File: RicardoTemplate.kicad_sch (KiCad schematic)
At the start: 39 parts, among them J1 RBUS, U1 ESP32-S3, Y1 R940000171

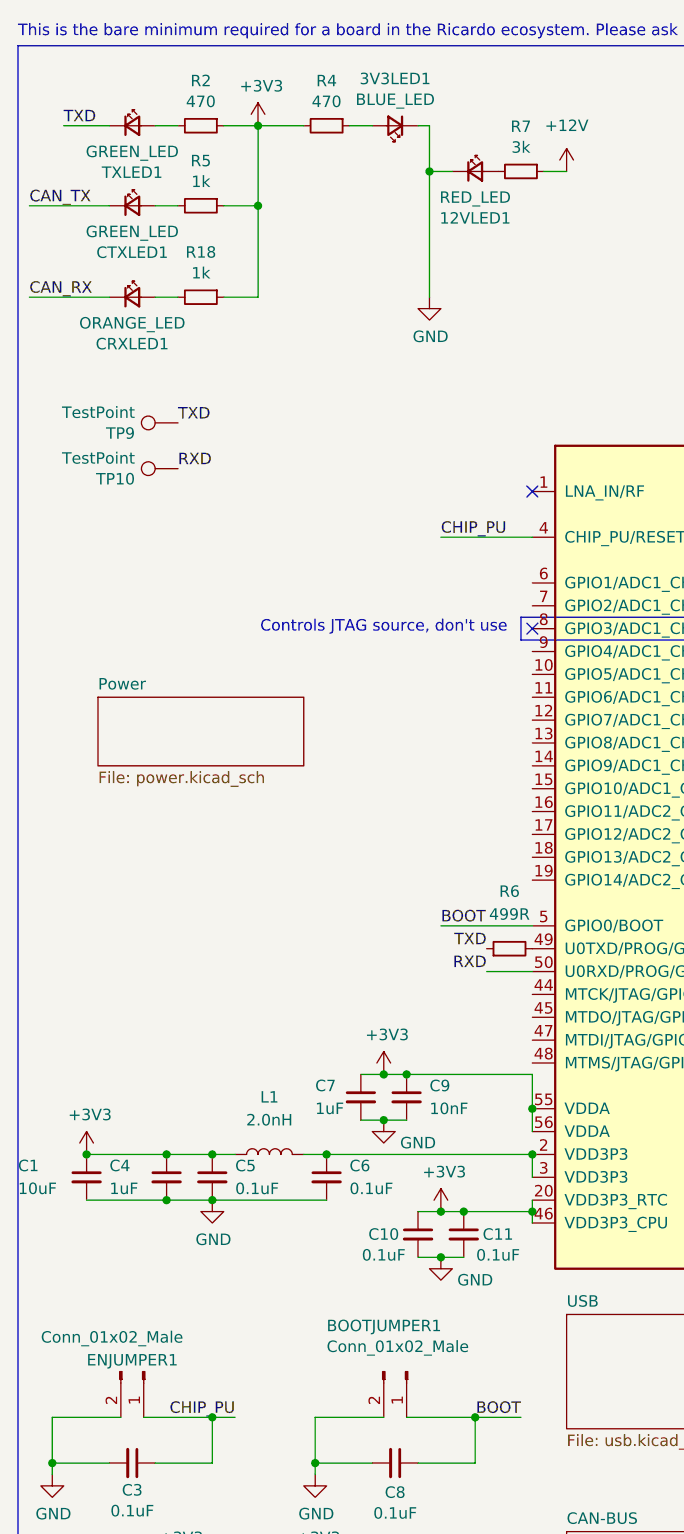
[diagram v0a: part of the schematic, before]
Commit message: Fixed LED footprints assigned as resistors, added gitignore for locks and backups
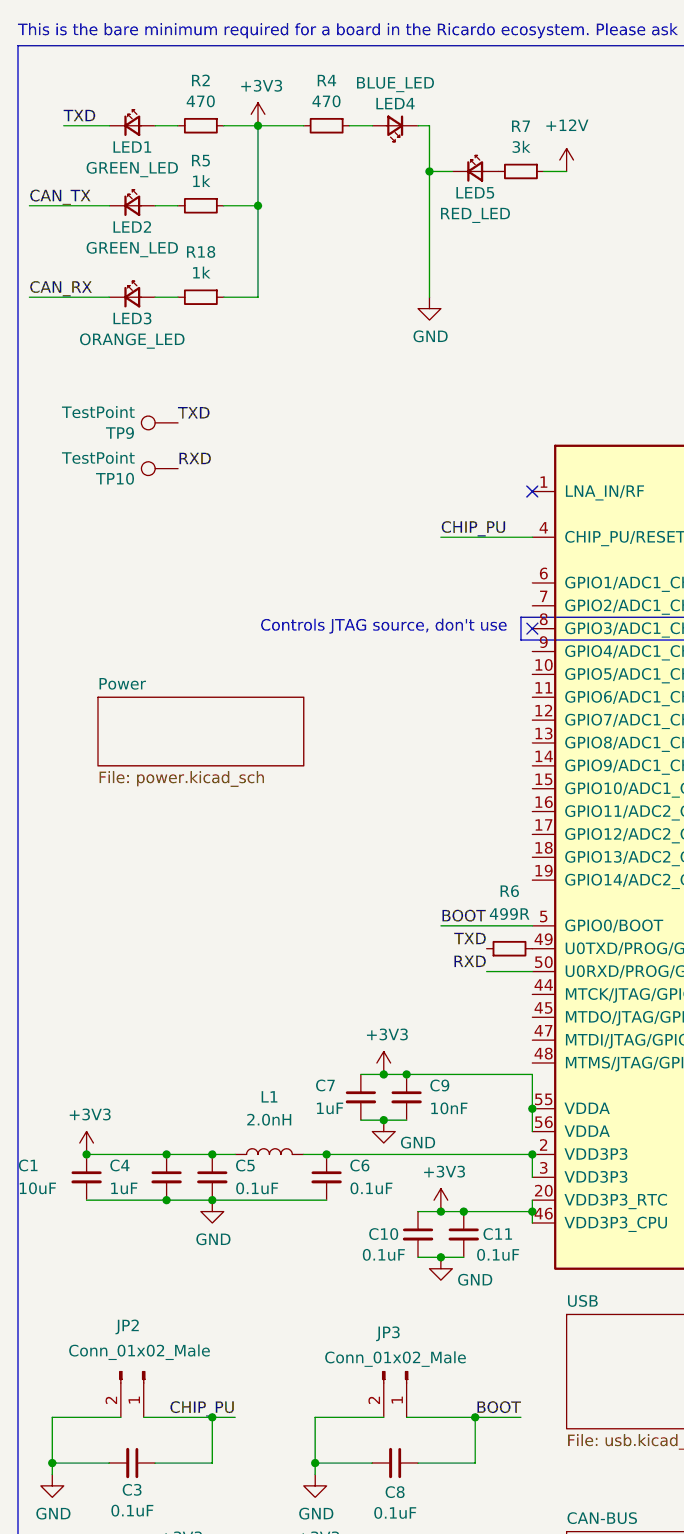
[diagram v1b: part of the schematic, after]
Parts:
- LED1: renamed from TXLED1; footprint Resistor_SMD:R_0402_1005Metric -> LED_SMD:LED_0402_1005Metric
- LED4: renamed from 3V3LED1; footprint Resistor_SMD:R_0402_1005Metric -> LED_SMD:LED_0402_1005Metric
- LED5: renamed from 12VLED1; footprint Resistor_SMD:R_0402_1005Metric -> LED_SMD:LED_0402_1005Metric
- renumbered ENJUMPER1 to JP2, BOOTJUMPER1 to JP3, CTXLED1 to LED2, CRXLED1 to LED3

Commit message: Fixed some footprint assignments, tidies up layout
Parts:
- J1: footprint Connector_Molex:Molex_Mini-Fit_Jr_5569-06A2_2x03_P4.20mm_Horizontal -> iclr:Molex_Mini-Fit_Jr_5569-06A2_2x03_P4.20mm_Horizontal
- LED2, LED3: footprint Resistor_SMD:R_0402_1005Metric -> LED_SMD:LED_0402_1005Metric
- Y1: footprint Crystal:Crystal_SMD_2016-4Pin_2.0x1.6mm -> iclr:Crystal_SMD_2016-4Pin_2.0x1.6mm
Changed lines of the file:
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@@
 (kicad_sch
-	(version 20231120)
+	(version 20250114)
 	(generator "eeschema")
-	(generator_version "8.0")
+	(generator_version "9.0")
 	(paper "A4")
+	(rectangle
+		(start 115.57 76.2)
+		(end 137.16 93.98)
+		(stroke
+			(width 0)
+			(type default)
+		)
+		(fill
+			(type none)
+		)
+	)
+	(text "Controls bootmode, don't use.\n"
+		(exclude_from_sim no)
+		(at 138.5894 113.9757 0)
+		(effects
+			(font
+				(size 1.27 1.27)
+			)
+			(justify left bottom)
+		)
+	)
+	(text "This is the bare minimum required for a board in the Ricardo ecosystem. Please ask before changing or removing anything in this box.\n\n"
+		(exclude_from_sim no)
+		(at 12.7 13.97 0)
+		(effects
+			(font
+				(size 1.27 1.27)
+			)
+			(justify left bottom)
+		)
+	)
+	(text "CAN + is CAN High\nCAN - is CAN LOW\nNamed with a + and - as it\nis a KiCad requirement to\nroute differential tracks\n"
+		(exclude_from_sim no)
+		(at 123.19 195.58 0)
+		(effects
+			(font
+				(size 1.27 1.27)
+			)
+			(justify left bottom)
+		)
+	)
+	(text "Controls JTAG source, don't use\n"
+		(exclude_from_sim no)
+		(at 67.0857 78.0878 0)
+		(effects
+			(font
+				(size 1.27 1.27)
+			)
+			(justify right bottom)
+		)
+	)
+	(text "Reserved for \nintegrated flash"
+		(exclude_from_sim no)
+		(at 112.776 84.328 90)
+		(effects
+			(font
+				(size 1.27 1.27)
+			)
+		)
+	)
 	(junction
 		(at 39.37 21.59)
@@
 		)
 	)
-	(rectangle
-		(start 115.57 76.2)
-		(end 137.16 93.98)
-		(stroke
-			(width 0)
-			(type default)
-		)
-		(fill
-			(type none)
-		)
-	)
-	(text "Controls bootmode, don't use.\n"
-		(exclude_from_sim no)
-		(at 138.5894 113.9757 0)
-		(effects
-			(font
-				(size 1.27 1.27)
-			)
-			(justify left bottom)
-		)
-	)
-	(text "This is the bare minimum required for a board in the Ricardo ecosystem. Please ask before changing or removing anything in this box.\n\n"
-		(exclude_from_sim no)
-		(at 12.7 13.97 0)
-		(effects
-			(font
-				(size 1.27 1.27)
-			)
-			(justify left bottom)
-		)
-	)
-	(text "CAN + is CAN High\nCAN - is CAN LOW\nNamed with a + and - as it\nis a KiCad requirement to\nroute differential tracks\n"
-		(exclude_from_sim no)
-		(at 123.19 195.58 0)
-		(effects
-			(font
-				(size 1.27 1.27)
-			)
-			(justify left bottom)
-		)
-	)
-	(text "Controls JTAG source, don't use\n"
-		(exclude_from_sim no)
-		(at 67.0857 78.0878 0)
-		(effects
-			(font
-				(size 1.27 1.27)
-			)
-			(justify right bottom)
-		)
-	)
-	(text "Reserved for \nintegrated flash"
-		(exclude_from_sim no)
-		(at 112.776 84.328 90)
-		(effects
-			(font
-				(size 1.27 1.27)
-			)
-		)
-	)
 	(label "CHIP_PU"
 		(at 36.83 165.1 180)
@@
 			)
 		)
-		(property "Footprint" "Connector_Molex:Molex_Mini-Fit_Jr_5569-06A2_2x03_P4.20mm_Horizontal"
+		(property "Footprint" "iclr:Molex_Mini-Fit_Jr_5569-06A2_2x03_P4.20mm_Horizontal"
 			(at 123.19 20.32 0)
 			(effects
@@
 			)
 		)
-		(property "Footprint" "Resistor_SMD:R_0402_1005Metric"
+		(property "Footprint" "LED_SMD:LED_0402_1005Metric"
 			(at 25.4 30.48 90)
 			(effects
@@
 			)
 		)
-		(property "Footprint" "Resistor_SMD:R_0402_1005Metric"
+		(property "Footprint" "LED_SMD:LED_0402_1005Metric"
 			(at 25.4 40.64 90)
 			(effects
@@
 			)
 		)
-		(property "Footprint" "Crystal:Crystal_SMD_2016-4Pin_2.0x1.6mm"
+		(property "Footprint" "iclr:Crystal_SMD_2016-4Pin_2.0x1.6mm"
 			(at 156.21 132.08 0)
 			(effects
@@
 		(at 73.66 153.67)
 		(size 25.4 12.7)
+		(exclude_from_sim no)
+		(in_bom yes)
+		(on_board yes)
+		(dnp no)
 		(fields_autoplaced yes)
 		(stroke
@@
 		(at 73.66 177.8)
 		(size 34.29 15.24)
+		(exclude_from_sim no)
+		(in_bom yes)
+		(on_board yes)
+		(dnp no)
 		(fields_autoplaced yes)
 		(stroke
@@
 		(at 21.59 85.09)
 		(size 22.86 7.62)
+		(exclude_from_sim no)
+		(in_bom yes)
+		(on_board yes)
+		(dnp no)
 		(fields_autoplaced yes)
 		(stroke
@@
 		)
 	)
+	(embedded_fonts no)
 )
